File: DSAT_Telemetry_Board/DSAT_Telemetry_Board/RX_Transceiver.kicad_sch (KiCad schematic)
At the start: 9 parts

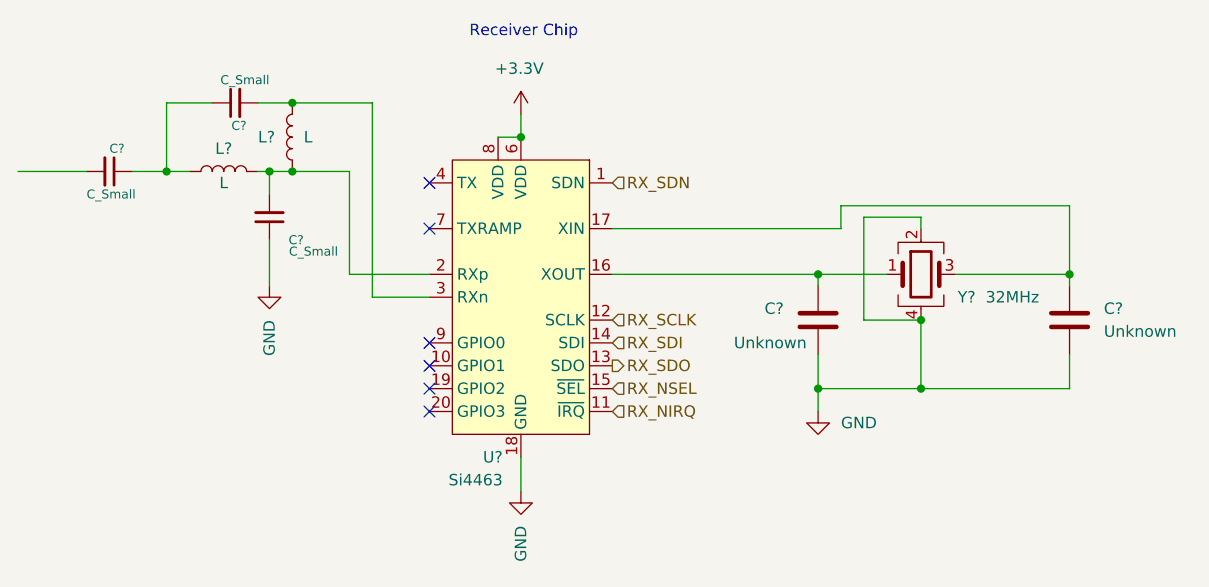
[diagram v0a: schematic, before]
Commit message: Seperate Branch
Updated Pin names, Added LNA, Fixed Pins on USB connection
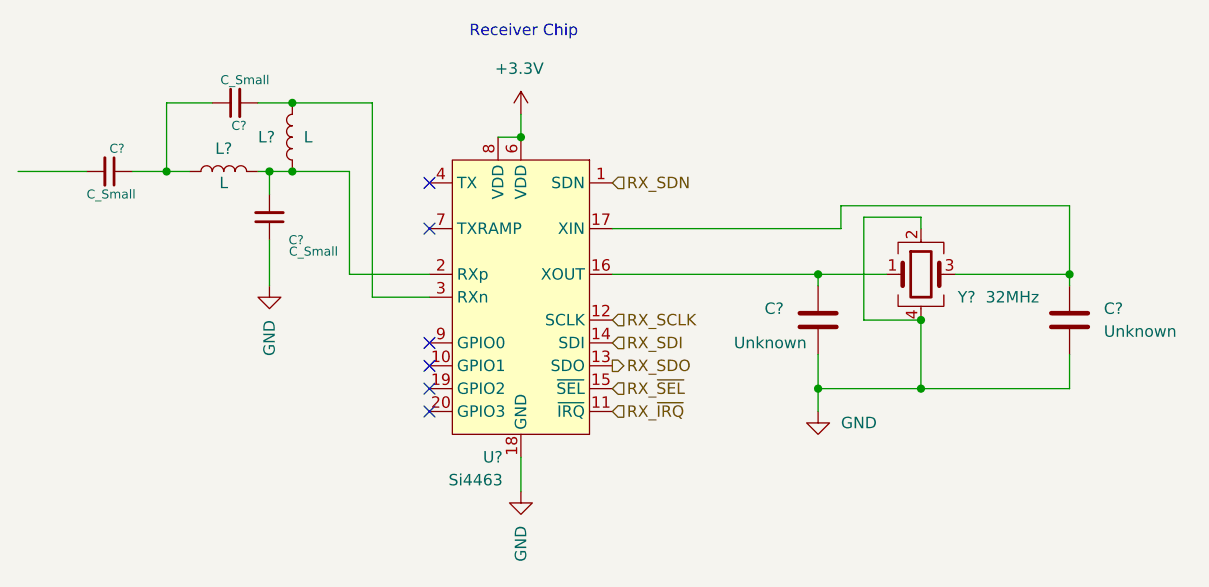
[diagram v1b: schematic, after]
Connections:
- net RX_NIRQ renamed RX_~{IRQ}
- net RX_NSEL renamed RX_~{SEL}
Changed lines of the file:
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@@
     (effects (font (size 1.27 1.27)) (justify left))
   )
-  (hierarchical_label "RX_NIRQ" (shape input) (at 137.16 100.33 0)
+  (hierarchical_label "RX_~{IRQ}" (shape input) (at 137.16 100.33 0)
     (effects (font (size 1.27 1.27)) (justify left))
   )
@@
     (effects (font (size 1.27 1.27)) (justify left))
   )
-  (hierarchical_label "RX_NSEL" (shape input) (at 137.16 97.79 0)
+  (hierarchical_label "RX_~{SEL}" (shape input) (at 137.16 97.79 0)
     (effects (font (size 1.27 1.27)) (justify left))
   )
